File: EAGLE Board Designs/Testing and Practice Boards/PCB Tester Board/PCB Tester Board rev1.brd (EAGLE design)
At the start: 160 x 100 mm, 147 parts, among them J1 JUMPER.1, J4 JUMPER.1, Q1 P-CHANNEL_MOSFET_DMP3099L-7, Q13 P-CHANNEL_MOSFET_DMP3099L-7, Q15 P-CHANNEL_MOSFET_DMP3099L-7, Q21 P-CHANNEL_MOSFET_DMP3099L-7, Q24 P-CHANNEL_MOSFET_DMP3099L-7, Q26 P-CHANNEL_MOSFET_DMP3099L-7, Q4 P-CHANNEL_MOSFET_DMP3099L-7, Q7 P-CHANNEL_MOSFET_DMP3099L-7, U1 AD5263, X1 CONNECTOR-6NANO-FIT_VERTICAL-6, X2 CONNECTOR-2, X3 CONNECTOR-6NANO-FIT_VERTICAL-6, X4 CONNECTOR-4NANO-FIT-VERTICAL-4, X5 CONNECTOR-4NANO-FIT-VERTICAL-4, X6 CONNECTOR-2NANO-FIT_VERTICAL-2, X7 CONNECTOR-2NANO-FIT_VERTICAL-2, X8 CONNECTOR-2NANO-FIT_VERTICAL-2, X9 CONNECTOR-2NANO-FIT_VERTICAL-2

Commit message: Rearranged and added more Wheel speed testers
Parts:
- removed U1: AD5263, HyTechDevices:TSSOP-24
- removed X2: CONNECTOR-2, HyTechDevices:MINIFIT_5566-2
- added C21, C25, C29: 10uF, HyTechDevices:0603-CAP
- added C22, C24, C26, C28, C30, C32: 1.5uF, HyTechDevices:0603-CAP
- added C23, C27, C31: 1 uF, HyTechDevices:0603-CAP
- added R63, R64, R65, R66, R72, R73, R74, R75, R81, R82, R83, R84: 715, HyTechDevices:0603-RES
- added R67, R76, R85: 100k, HyTechDevices:0603-RES
- added R68, R69, R70, R71, R77, R78, R79, R80, R86, R87, R88, R89: 1k, HyTechDevices:0603-RES
- added U$25, U$27, U$29: NA555SO-8, HyTechDevices:SOIC-08
- added U$26, U$28: NE5532SOIC, HyTechDevices:SOIC-08
- added U2: AD5263, HyTechDevices:TSSOP-24
- U$19: value MMBZ5245BTS-7-F -> NE5532SOIC; device HyTechDevices:SOT363 -> HyTechDevices:SOIC-08
- moved R27 282.7 mm to (-108.0, -172.7)
- moved R19 282.5 mm to (-108.0, -165.1)
- moved R23 282.2 mm to (-108.0, -168.9)
- moved R24 280.5 mm to (-104.1, -168.9)
- moved R20 280.4 mm to (-104.1, -165.1)
- moved R25 279.0 mm to (-100.3, -168.9)
- moved R21 278.5 mm to (-100.3, -165.1)
- moved R26 277.7 mm to (-96.5, -168.9)
- moved R22 276.7 mm to (-96.5, -165.1)
- moved C5 276.3 mm to (-100.3, -161.3)
- moved C7 273.0 mm to (-96.5, -161.3)
- moved C3 261.0 mm to (-108.0, -161.3)
- moved C4 260.2 mm to (-104.1, -161.3)
- moved U$13 236.6 mm to (-105.4, -154.9)
- moved U$15 234.2 mm to (-97.8, -154.9)
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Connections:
- net ALTERNATINGVOLTAGE renamed ALTERNATINGVOLTAGE2
- removed net SENSOROUT: R20.1, R22.2, U$13.5, X2.2
- new net ALTERNATINGVOLTAGE1: R66.1, R71.1, U$19.1
- new net ALTERNATINGVOLTAGE3: R75.1, R80.1, U$26.1
- new net ALTERNATINGVOLTAGE4: R84.1, R89.1, U$28.1
- new net N$17: R69.2, U$25.3, U2.2
- new net N$55: R68.1, R69.1, U$19.3
- new net N$56: R64.2, R65.2, U$19.7
- new net N$57: R70.1, R71.2, U$19.2
- new net N$58: C21.2, R67.1, U$25.2, U$25.6, U2.3
- new net N$59: C24.1, U$25.5
- new net N$60: C22.1, C24.2
- new net N$61: R63.2, R65.1, U$19.6
- new net N$62: R78.2, U$27.3
- new net N$63: R77.1, R78.1, U$26.3
- new net N$64: R73.2, R74.2, U$26.7
- new net N$65: R79.1, R80.2, U$26.2
- new net N$66: C25.2, R76.1, U$27.2, U$27.6
- new net N$67: C28.1, U$27.5
- new net N$68: C26.1, C28.2
- new net N$69: R72.2, R74.1, U$26.6
- new net N$70: R87.2, U$29.3
- new net N$71: R86.1, R87.1, U$28.3
- new net N$72: R82.2, R83.2, U$28.7
- new net N$73: R88.1, R89.2, U$28.2
- new net N$74: C29.2, R85.1, U$29.2, U$29.6
- new net N$75: C32.1, U$29.5
- new net N$76: C30.1, C32.2
- new net N$77: R81.2, R83.1, U$28.6
- new net WS1_IN: R20.1, R22.2, R64.1, R66.2, R73.1, R75.2, R82.1, R84.2, U$13.5, U$19.5, U$26.5, U$28.5
- net +12V: now also U$19.8, U$26.8, U$28.8
- net +5V: now also C23.2, C27.2, C31.2, R67.2, R68.2, R76.2, R77.2, R85.2, R86.2, U$25.4, U$25.8, U$27.4, U$27.8, U$29.4, U$29.8, U2.15, U2.7; no longer U1.15, U1.7
- net 555_GND: now also C21.1, C22.2, C25.1, C26.2, C29.1, C30.2, U$25.1, U$27.1, U$29.1; no longer U$19.P$6
- net CS: now also U2.13; no longer U1.13
- net GND: now also C23.1, C27.1, C31.1, R63.1, R70.2, R72.1, R79.2, R81.1, R88.2, U$19.4, U$26.4, U$28.4, U2.18, U2.8, U2.9; no longer U1.18, U1.8, U1.9
- net N$18: no longer U1.2
- net N$22: no longer U1.3
- net N$23: no longer U$19.P$5
- net RESET: now also U2.14; no longer U1.14
- net SCLK: now also U2.12; no longer U1.12
- net SDI: now also U2.11; no longer U1.11
- net SDO: now also U2.16; no longer U1.16

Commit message: Linked 555s to digipot and linked ground switch
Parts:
- moved R4 345.4 mm to (-108.0, -240.0)
- moved D4 332.8 mm to (-108.0, -236.2)
- moved Q3 331.5 mm to (-102.9, -236.2)
- moved R3 238.1 mm to (-105.4, -228.6)
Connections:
- removed net N$66: C25.2, R76.1, U$27.2, U$27.6
- new net N$82: C25.2, R76.1, U$27.2, U$27.6, U2.6
- new net WS2_IN: R20.1, R22.2, U$13.5
- new net WS3_IN: R73.1, R75.2, U$26.5
- new net WS4_IN: R82.1, R84.2, U$28.5
- net N$18: now also U2.23
- net N$22: now also U2.22
- net N$62: now also U2.5
- net N$70: now also U2.20
- net N$74: now also U2.19
- net WS1_IN: no longer R20.1, R22.2, R73.1, R75.2, R82.1, R84.2, U$13.5, U$26.5, U$28.5

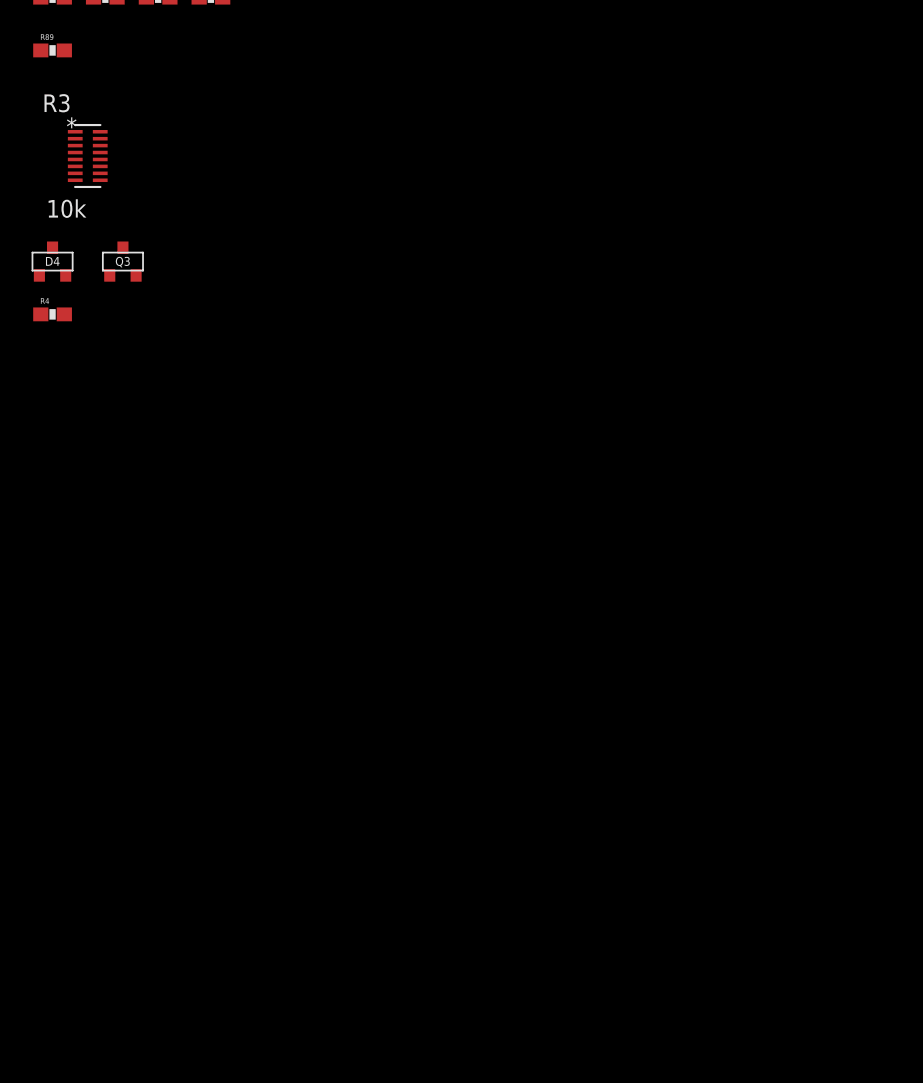
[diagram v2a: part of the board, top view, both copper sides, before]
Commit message: Added Fan 1A tester
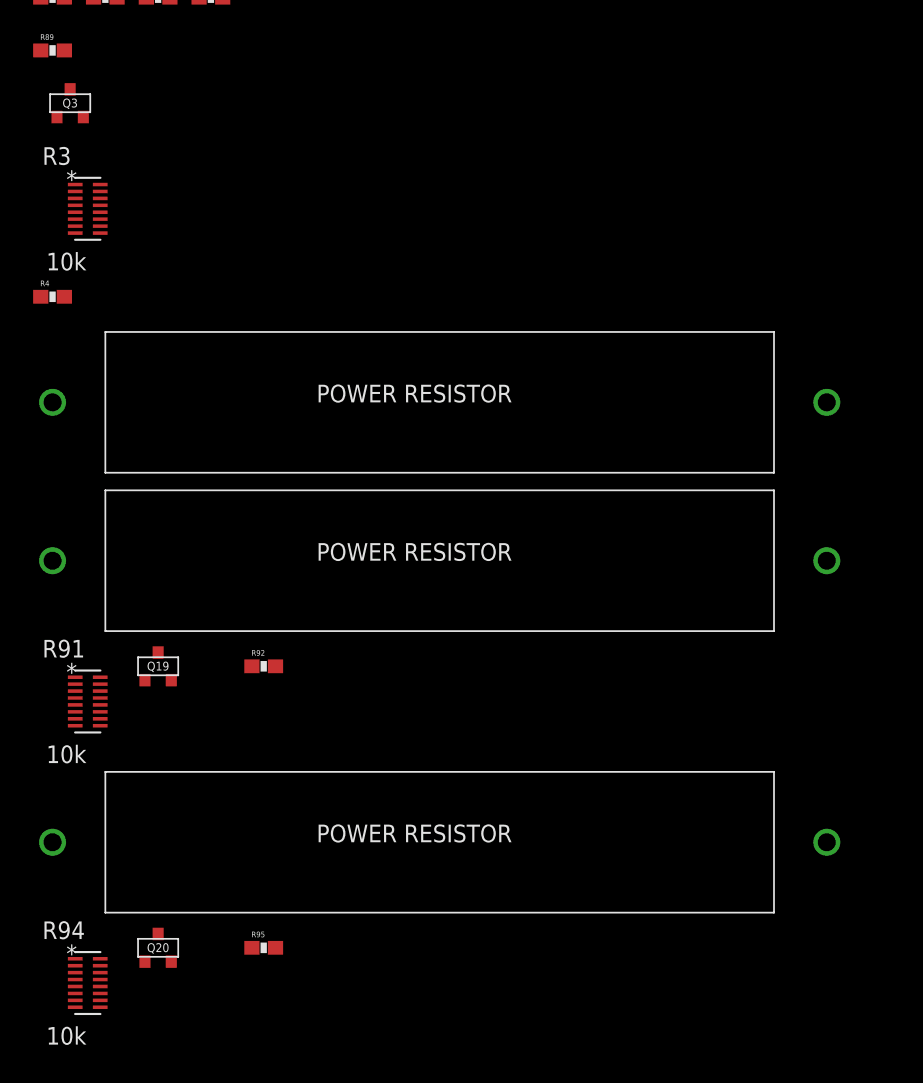
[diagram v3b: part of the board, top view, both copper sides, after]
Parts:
- removed D4: DIODE_ZENER, HyTechDevices:SOT23
- added Q19, Q20: P-CHANNEL_MOSFET_DMP3099L-7, HyTechDevices:SOT23
- added R90, R93, R96: 12k, HyTechDevices:10W_RESISTOR_VISHAY
- added R91, R94: 10k, HyTechDevices:YAG_YC248-M
- added R92, R95: 10, HyTechDevices:0603-RES
- Q3: value (none) -> P-CHANNEL_MOSFET_DMP3099L-7
- moved Q3 12.0 mm to (-106.7, -224.8)
- moved R3 3.81 mm to (-105.4, -232.4)
- moved R4 1.27 mm to (-108.0, -238.8)
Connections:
- removed net 555_CTRL: D4.3, R3.12, R4.1
- new net FAN_IN_1: R90.1
- new net FAN_IN_2: R93.1
- new net FAN_IN_3: R96.1
- new net FAN_TEST_CONTROL: R3.12, R4.1, R91.12, R92.1, R94.12, R95.1
- new net N$66: Q3.3, R90.2
- new net N$78: Q19.1, R92.2
- new net N$79: Q19.3, R93.2
- new net N$80: Q20.1, R95.2
- new net N$81: Q20.3, R96.2
- net +12V: now also Q19.2, Q20.2, Q3.2
- net 555_GND: no longer Q3.3
- net GND: now also R91.5, R94.5; no longer D4.1, Q3.2

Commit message: Updated libraries and zener diode arrays
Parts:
- removed X6, X7, X8, X9: CONNECTOR-2NANO-FIT_VERTICAL-2, HyTechDevices:NANO-FIT_VERTICAL-2
- D10: value DIODE_ZENER0805 -> DIODE_ZENER; device HyTechDevices:0805_D -> HyTechDevices:SOT23
- moved U$12 403.9 mm to (-106.7, -315.0)
- moved U$11 400.7 mm to (-106.7, -311.1)
- moved U$7 397.5 mm to (-106.7, -307.3)
- moved U$6 394.4 mm to (-106.7, -303.5)
- moved U$5 391.3 mm to (-106.7, -299.7)
- moved U$4 388.3 mm to (-106.7, -295.9)
- moved U$20 313.6 mm to (-106.7, -318.8)
- moved U$23 280.7 mm to (-106.7, -322.6)
- moved U$24 280.7 mm to (-106.7, -326.4)
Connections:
- removed net N$31: U$5.P$4
- net +12V: now also U$11.P$6, U$12.P$4, U$5.P$4, U$5.P$5; no longer U$12.P$5, U$12.P$6, U$7.P$5, U$7.P$6
- net BMS_OK: now also U$11.P$4; no longer U$11.P$6
- net BMS_OK_CTRL2: now also U$11.P$3; no longer U$12.P$3
- net DASH_12V_CTRL: now also U$4.P$4; no longer U$6.P$6
- net DASH_12V_CTRL2: now also U$5.P$1; no longer U$7.P$3
- net DIODE1: now also U$24.P$1; no longer U$24.P$3
- net DIODE3: now also U$24.P$3; no longer U$24.P$1
- net EXTRA_BTN_CTRL: now also U$7.P$5; no longer U$5.P$5
- net GND: now also U$11.P$1, U$7.P$1, U$7.P$2; no longer U$11.P$3, U$5.P$1, U$5.P$2, U$5.P$3
- net HV_12V_CTRL: now also U$23.P$6; no longer U$23.P$4
- net MARK_BTN_CTRL: now also U$6.P$4; no longer U$4.P$6
- net MC_CYCLE_BTN_CTRL: now also U$6.P$5; no longer U$4.P$5
- net MODE_BTN_CTRL: now also U$6.P$6; no longer U$4.P$4
- net N$50: now also U$23.P$4; no longer U$23.P$6
- net OKHS_CTRL2: now also U$12.P$1; no longer U$12.P$2
- net SHUTDOWN_H_CTRL: now also U$4.P$6; no longer U$6.P$4
- net SHUTDOWN_H_CTRL2: now also D10.1, U$5.P$3; no longer D10.A, U$7.P$1
- net SSOK: now also D10.3, U$5.P$6; no longer D10.C, U$7.P$4
- net SSOK_CTRL: now also U$4.P$5; no longer U$6.P$5
- net SSOK_CTRL2: now also U$5.P$2; no longer U$7.P$2
- net START_BTN_CTRL: now also U$7.P$4; no longer U$5.P$6
